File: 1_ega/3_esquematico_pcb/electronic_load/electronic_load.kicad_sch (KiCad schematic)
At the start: 54 parts, among them J1 Encoder, J10 5V, J11 LOAD, J12 Memoria SD, J14 INA219, J15 VCC, J16 LCD_I2C, J17 EGB_I2C, J18 EGB_UART, J2 RTC_I2C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

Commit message: feat: pcb v2
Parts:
- removed J16: LCD_I2C, Connector_PinHeader_2.54mm:PinHeader_1x02_P2.54mm_Vertical, symbol Connector:Conn_01x02_Pin
- removed J6: LCD_PWR, Connector_PinHeader_2.54mm:PinHeader_1x02_P2.54mm_Vertical, symbol Connector:Conn_01x02_Pin
- added HS1: Heatsink, electronic_load:Heatsink_2725D, symbol Mechanical:Heatsink
- added J13: LCD, Connector_Molex:Molex_KK-254_AE-6410-04A_1x04_P2.54mm_Vertical, symbol Connector:Conn_01x04_Pin
- C2, C5: footprint Capacitor_THT:C_Disc_D3.4mm_W2.1mm_P2.50mm -> Capacitor_THT:C_Disc_D5.0mm_W2.5mm_P5.00mm
- C6: footprint Capacitor_THT:CP_Radial_D6.3mm_P2.50mm -> Capacitor_THT:CP_Radial_D10.0mm_P3.50mm
- L1: footprint Inductor_THT:L_Radial_D10.5mm_P5.00mm_Abacron_AISR-01 -> Inductor_THT:L_Radial_D7.5mm_P3.50mm_Fastron_07P
- SW1, SW2: footprint Connector_PinHeader_2.54mm:PinHeader_1x02_P2.54mm_Vertical -> Connector_Molex:Molex_KK-254_AE-6410-02A_1x02_P2.54mm_Vertical
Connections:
- net +5V: now also J13.3 (Pin_3)
- net BTN_STOP: now also SW2.1; no longer SW2.2
- net GND: now also SW2.2, J13.4 (Pin_4); no longer SW2.1
- net I2C_SCL: now also A1.25 (GPIO19), J13.1 (Pin_1); no longer A1.22 (GPIO17)
- net I2C_SDA: now also A1.24 (GPIO18), J13.2 (Pin_2); no longer A1.21 (GPIO16)
- net LED_ACTIVE: now also A1.20 (GPIO15); no longer A1.29 (GPIO22)
- net MOS_PWM: now also A1.21 (GPIO16); no longer A1.24 (GPIO18)
- net RTC_32K: now also A1.27 (GPIO21)
- net RTC_SQW: now also A1.26 (GPIO20)
- net TEMP_DIODE: now also U1.7; no longer U1.1
- net at C2.1, R6.2: now also U1.3 (+); no longer U1.5 (+)
- net at R11.1, R12.2: now also U1.2 (-); no longer U1.6 (-)
- net at R14.1, R15.1: now also U1.6 (-); no longer U1.2 (-)
- net at D2.2 (A), Q3.1 (C): now also U1.5 (+); no longer U1.3 (+)
- net at R11.2, R18.2: now also U1.1; no longer U1.7
- no-connect marks 13 -> 11
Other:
- moved on the sheet: U1A, U1B

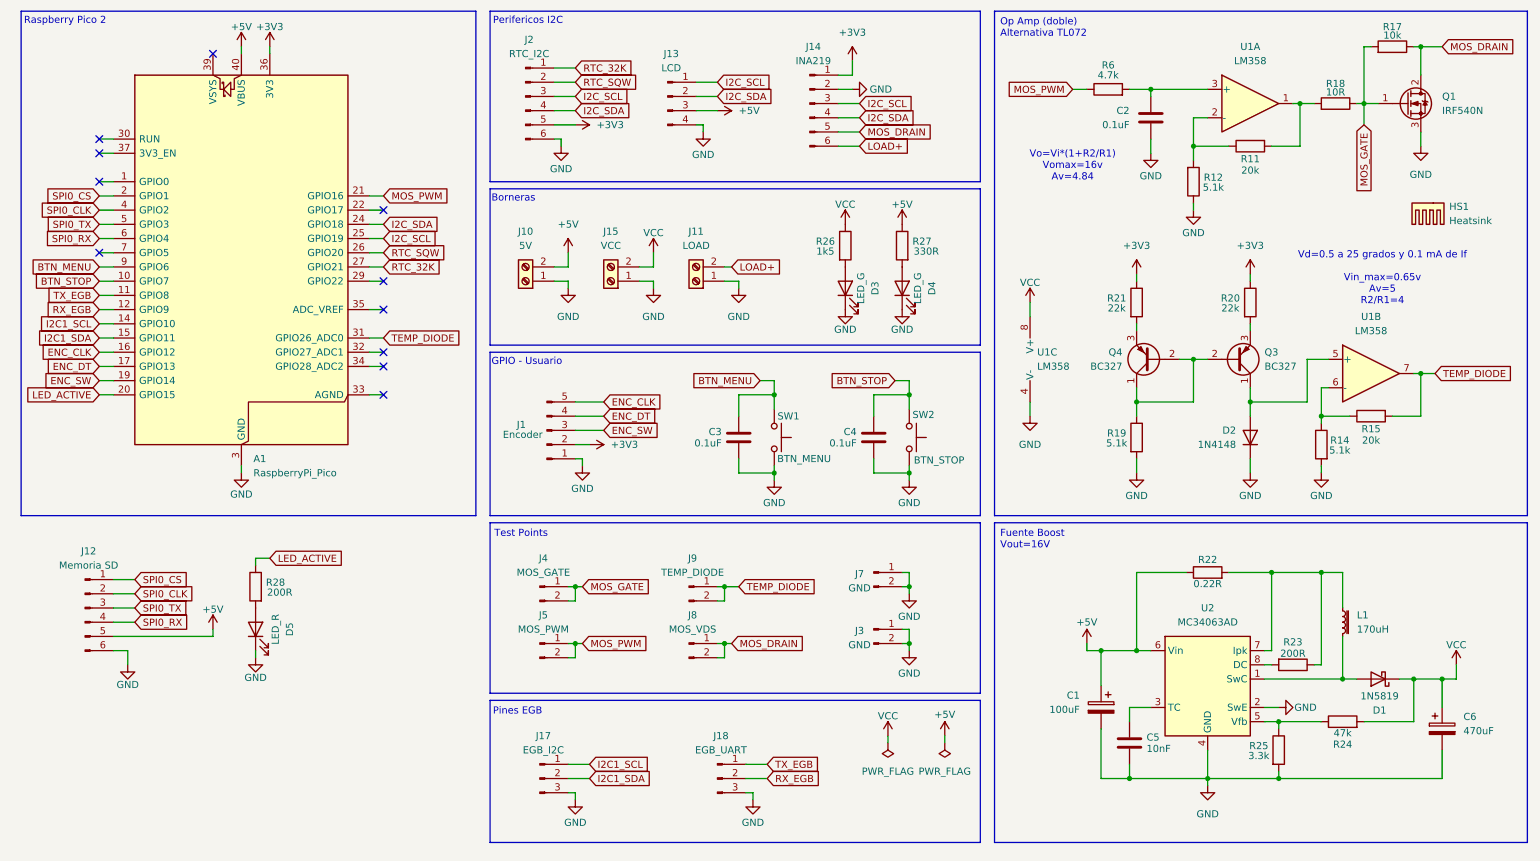
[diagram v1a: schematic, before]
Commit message: chore: add mounting hole to pcb
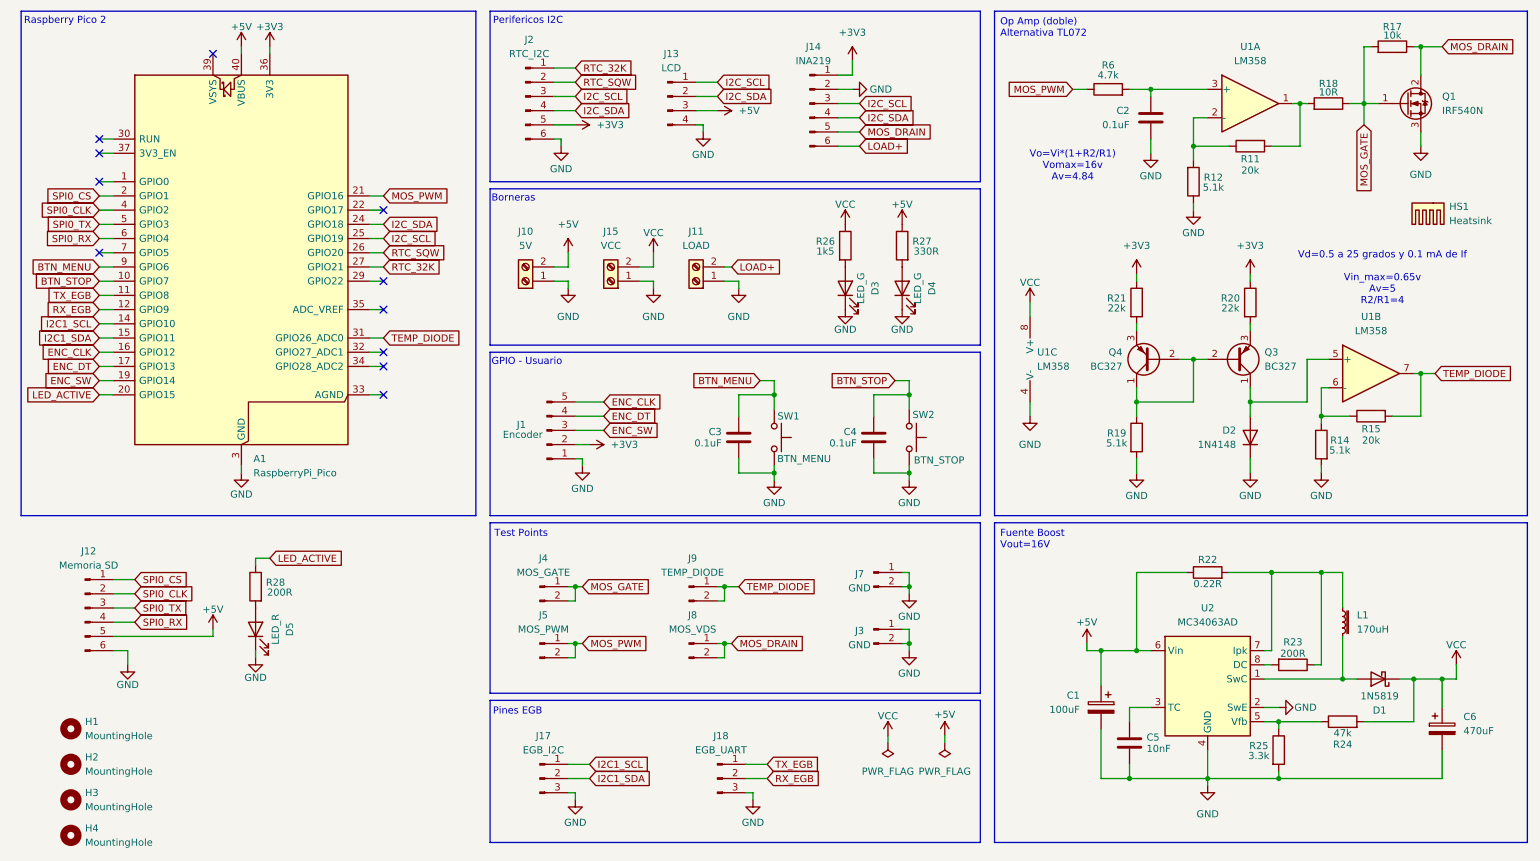
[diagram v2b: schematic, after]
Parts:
- added H1, H2, H3, H4: MountingHole, MountingHole:MountingHole_3.2mm_M3_DIN965, symbol Mechanical:MountingHole
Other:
- moved on the sheet: R18

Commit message: chore: add pdfs
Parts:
- L1: value 170uH -> 220 uH
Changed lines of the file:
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@@
 			)
 		)
-		(property "Value" "170uH"
+		(property "Value" "220 uH"
 			(at 252.73 124.4599 0)
 			(effects

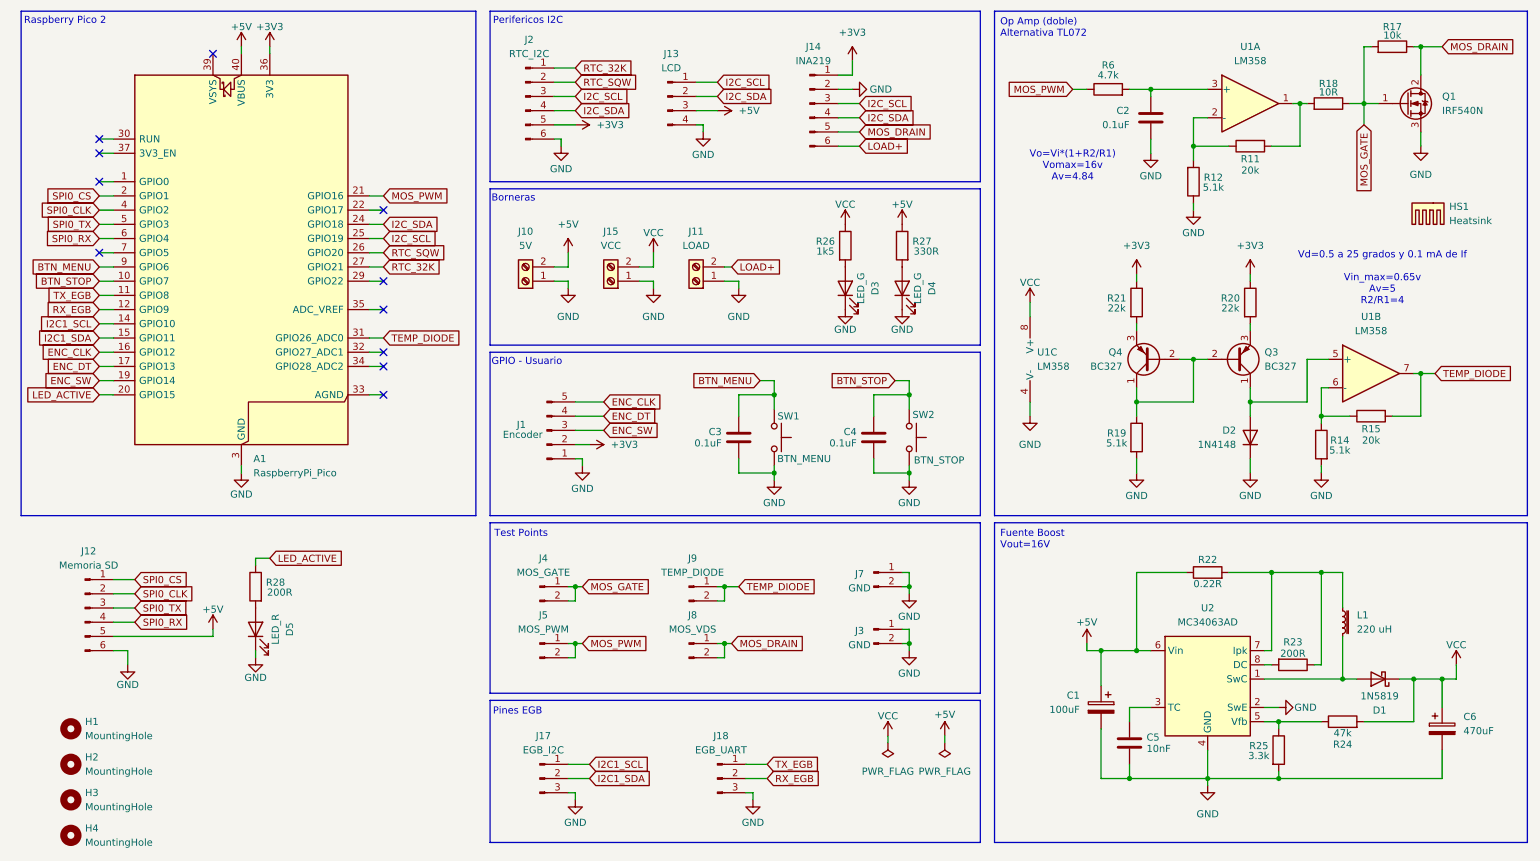
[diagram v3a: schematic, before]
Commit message: minor changes to pcb MOSFET position
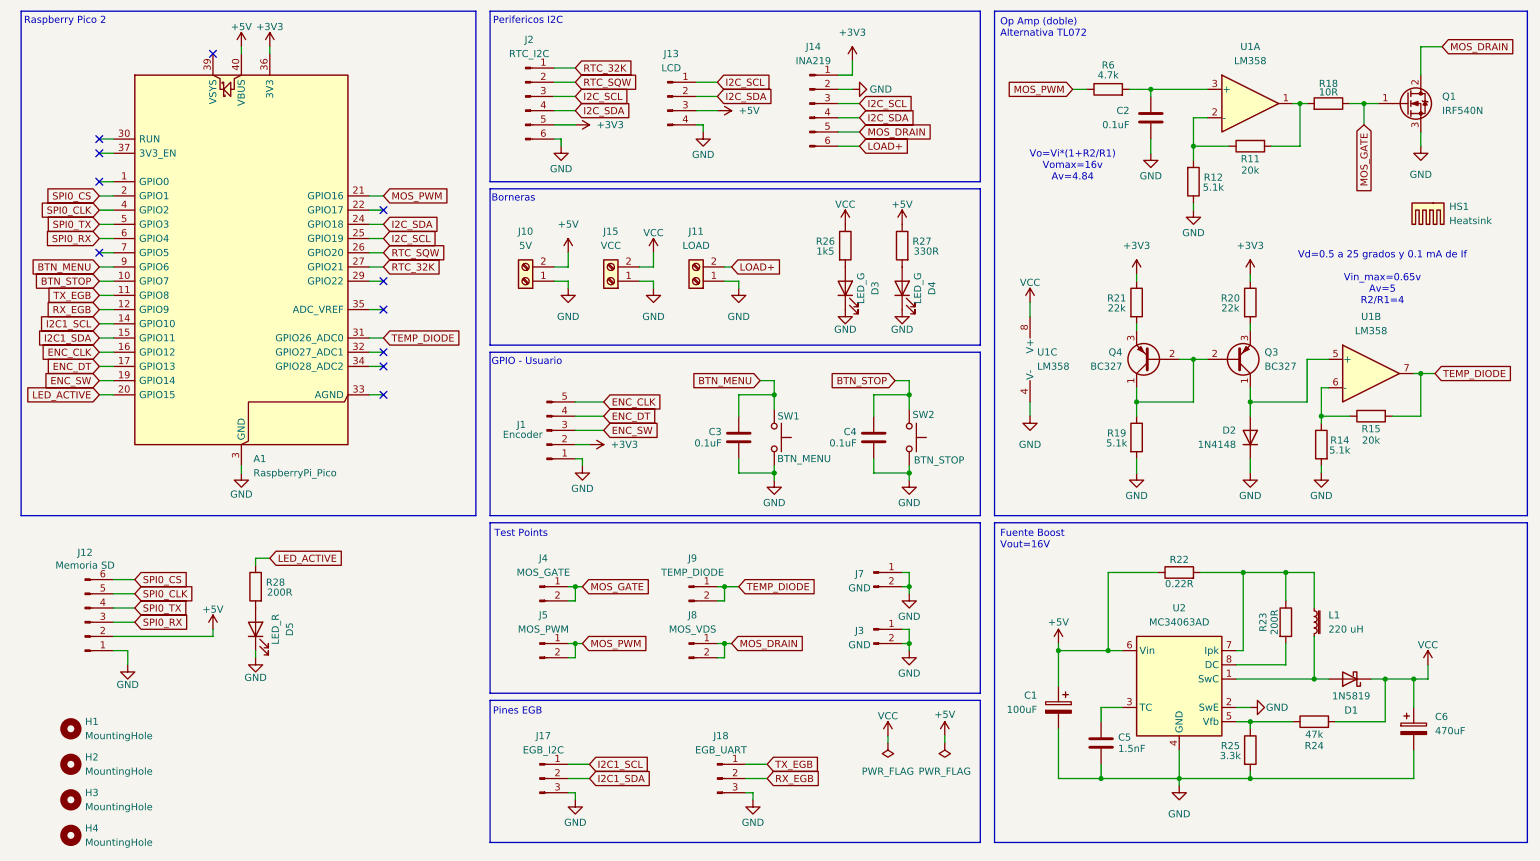
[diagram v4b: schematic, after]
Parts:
- removed R17: 10k, Resistor_THT:R_Axial_DIN0207_L6.3mm_D2.5mm_P10.16mm_Horizontal, symbol Device:R
- C5: value 10nF -> 1.5nF
- HS1: footprint electronic_load:Heatsink_2725D -> Heatsink:Heatsink_Fischer_FK224xx2201_25x8.3mm
- J12: footprint Connector_PinSocket_2.54mm:PinSocket_1x06_P2.54mm_Vertical -> Connector_Molex:Molex_KK-254_AE-6410-06A_1x06_P2.54mm_Vertical
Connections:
- net +5V: now also J12.2 (Pin_2); no longer J12.5 (Pin_5)
- net GND: now also J12.1 (Pin_1); no longer J12.6 (Pin_6)
- net SPI0_CLK: now also J12.5 (Pin_5); no longer J12.2 (Pin_2)
- net SPI0_CS: now also J12.6 (Pin_6); no longer J12.1 (Pin_1)
- net SPI0_RX: now also J12.3 (Pin_3); no longer J12.4 (Pin_4)
- net SPI0_TX: now also J12.4 (Pin_4); no longer J12.3 (Pin_3)
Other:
- moved on the sheet: C1, C5, C6, D1, L1, R22, R23, R24, R25

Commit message: add rtc and pcb changes
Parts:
- added F1: Fuse, Fuse:Fuseholder_Clip-5x20mm_Eaton_1A5601-01_Inline_P20.80x6.76mm_D1.70mm_Horizontal, symbol Device:Fuse
- HS1: footprint Heatsink:Heatsink_Fischer_FK224xx2201_25x8.3mm -> electronic_load:Heatsink_2725D
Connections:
- net LOAD+: now also F1.2; no longer J11.2 (Pin_2)
- new net: F1.1, J11.2 (Pin_2)
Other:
- moved on the sheet: C2, D3, D4, HS1, Q1, R11, R12, R18, R26, R27, R6, U1A

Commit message: Update last version of pcb
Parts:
- added RV1: 1k, Connector_PinHeader_2.54mm:PinHeader_1x03_P2.54mm_Vertical, symbol Device:R_Potentiometer
- added RV2: 5k, Connector_PinHeader_2.54mm:PinHeader_1x03_P2.54mm_Vertical, symbol Device:R_Potentiometer
- C6: value 470uF -> 330uF
- R11: value 20k -> 5.1k
- R12: value 5.1k -> 12k
- R26: value 1k5 -> 2.2k
- R28: value 200R -> 150R
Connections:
- net at R11.1, U1.2 (-): now also RV2.1, RV2.2; no longer R12.2
- net at R24.1, U2.5 (Vfb): now also RV1.1; no longer R25.1
- new net: R25.1, RV1.2, RV1.3
- new net: R12.2, RV2.3
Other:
- moved on the sheet: C1, C5, C6, D1, D2, L1, Q3, Q4, R11, R12, R14, R15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

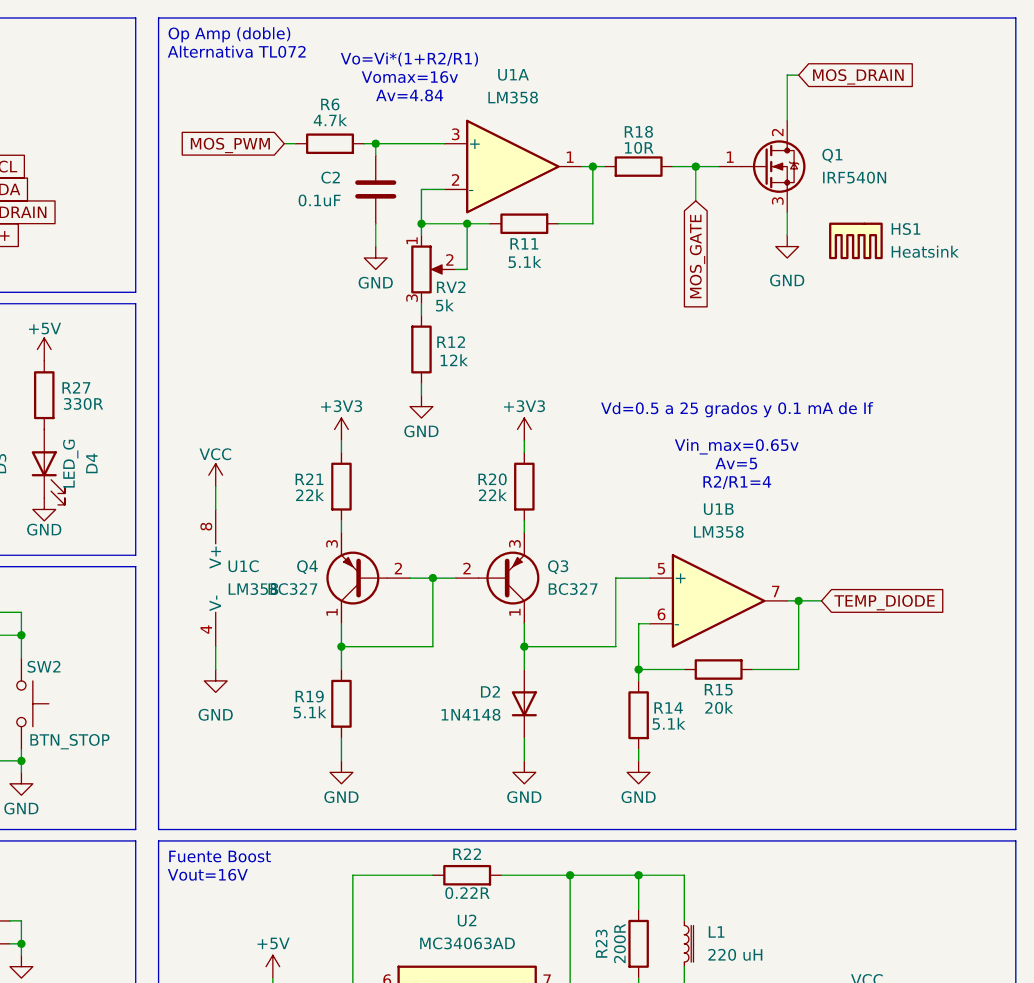
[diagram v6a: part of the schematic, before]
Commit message: add temperature info in PID menu
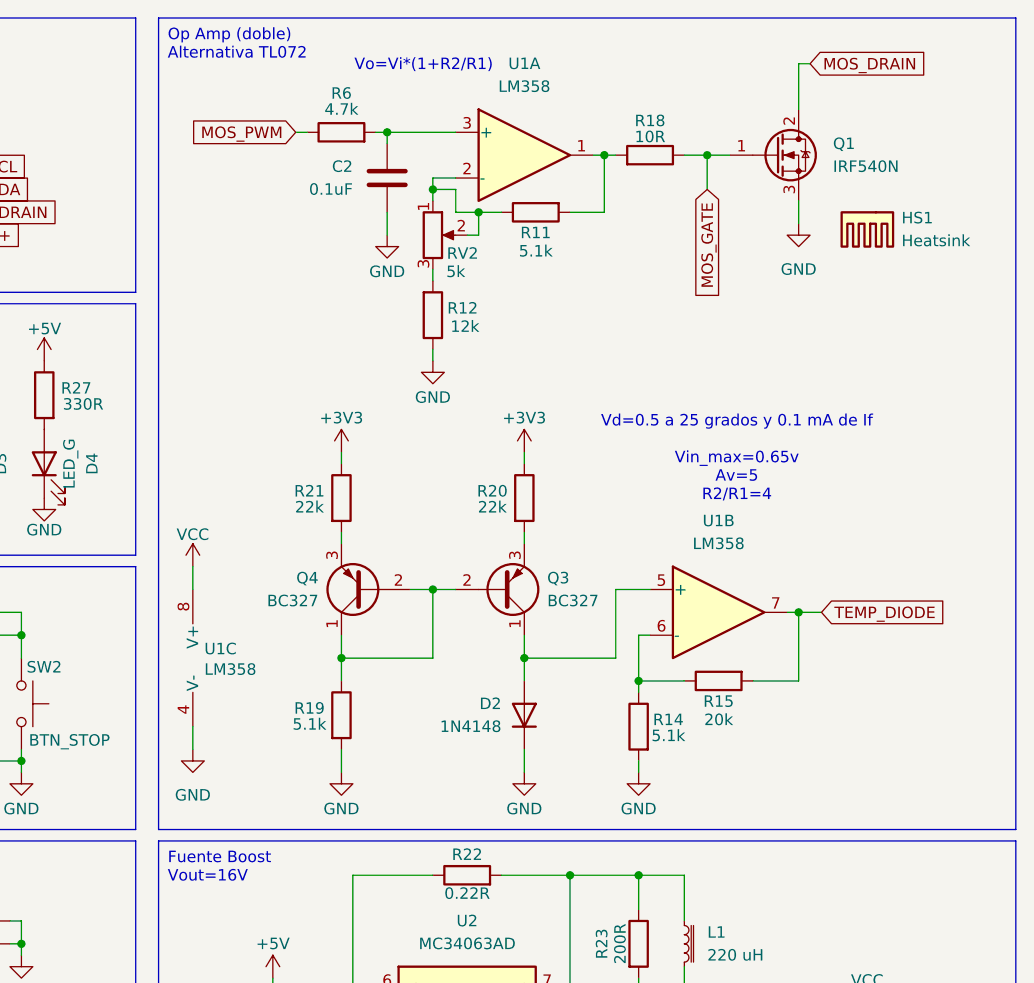
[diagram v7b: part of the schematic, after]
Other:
- note added: "Vo=Vi*(1+R2/R1)"
- note removed: "Vo=Vi*(1+R2/R1) Vomax=16v Av=4.84"
- moved on the sheet: C2, D2, HS1, Q1, Q3, Q4, R11, R12, R14, R15, R18, R19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

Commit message: chore: update PCB pdf to final version
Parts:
- J1: footprint Connector_PinHeader_2.54mm:PinHeader_1x05_P2.54mm_Vertical -> Connector_Molex:Molex_KK-254_AE-6410-05A_1x05_P2.54mm_Vertical
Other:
- company: (none) -> Pablo Gomez
- title: (none) -> Carga Electrónica Programable
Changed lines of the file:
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@@
 	(generator_version "9.0")
 	(paper "A4")
+	(title_block
+		(title "Carga Electrónica Programable")
+		(date "2025-08-18")
+		(rev "v1")
+		(company "Pablo Gomez")
+		(comment 1 "Nicolas Pereyra")
+	)
 	(rectangle
 		(start 97.79 74.93)
@@
 			)
 		)
-		(property "Footprint" "Connector_PinHeader_2.54mm:PinHeader_1x05_P2.54mm_Vertical"
+		(property "Footprint" "Connector_Molex:Molex_KK-254_AE-6410-05A_1x05_P2.54mm_Vertical"
 			(at 107.95 88.9 0)
 			(effects
